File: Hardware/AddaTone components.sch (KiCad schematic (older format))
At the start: 82 parts, among them J1 SWD_Header, J2 Conn_01x20_Female, J3 Conn_01x20_Female, J8 Eurorack_16_pin_power, U1 STM32F446RETx, U2 ICE40UP5K-SG48ITR, U3 MCP6004, U4 PCM5100APW, U5 TL072, U6 LD1117S12TR_SOT223, U7 LM1117-3.3, Y1 ECS-12MHz

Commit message: Initial PCB Wiring Completed
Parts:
- C1, C15, C35, C4, C7, C9: footprint Capacitors_SMD:C_0805_HandSoldering -> Capacitors_SMD:C_0603_HandSoldering
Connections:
- net labels added: FPGA_SO
- wire segments 370 -> 367
- no-connect marks 54 -> 57

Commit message: Updated microcontroller code for correct ADC channels and implemented HSE oscillator output
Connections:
- net labels added: FREQ_SCALE_CV, HARM_COUNT_POT, PITCH_CV
- net labels removed: FREQ_SCALE, HARM_COUNT, V_OCT_CV
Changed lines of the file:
@@
 $EndComp
 Text GLabel 9750 2350 2    50   Input ~ 0
-V_OCT_CV
+PITCH_CV
 Wire Wire Line
 	9750 2350 9400 2350
@@
 	8350 3600 8400 3600
 Text GLabel 3400 2600 2    50   Input ~ 0
-V_OCT_CV
+PITCH_CV
 Text GLabel 1650 3900 0    50   Input ~ 0
 HARM1_CV
@@
 DAC2_OUT
 Text GLabel 3400 2200 2    50   Input ~ 0
-HARM_COUNT
+HARM_COUNT_POT
 $Comp
 L Amplifier_Operational:MCP6004 U3
@@
 $EndComp
 Text GLabel 9750 7950 2    50   Input ~ 0
-FREQ_SCALE
+FREQ_SCALE_CV
 Wire Wire Line
 	9750 6050 9400 6050
@@
 	15700 4600 15850 4600
 Text GLabel 3400 2700 2    50   Input ~ 0
-FREQ_SCALE
+FREQ_SCALE_CV
 Wire Wire Line
 	3250 2600 3400 2600
@@
 HARM2_POT
 Text GLabel 6250 1100 0    50   Input ~ 0
-HARM_COUNT
+HARM_COUNT_POT
 Text GLabel 6250 1300 0    50   Input ~ 0
 FTUNE

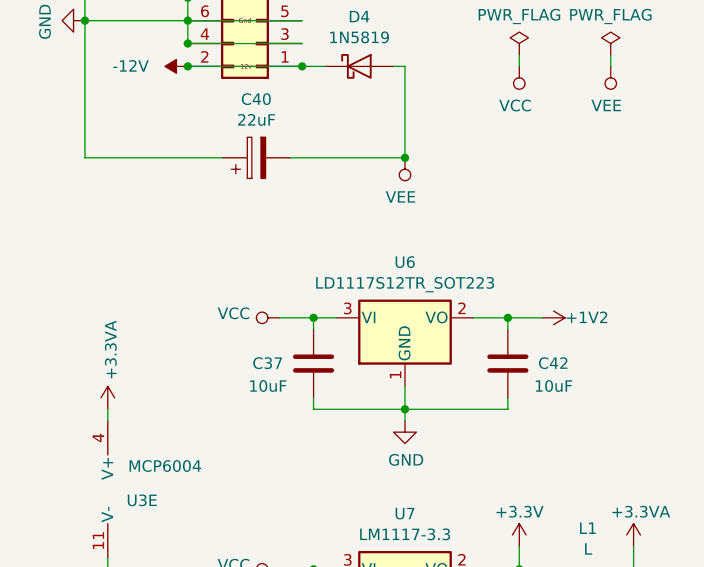
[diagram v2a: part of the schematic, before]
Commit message: Minor tweaks to PCB layout
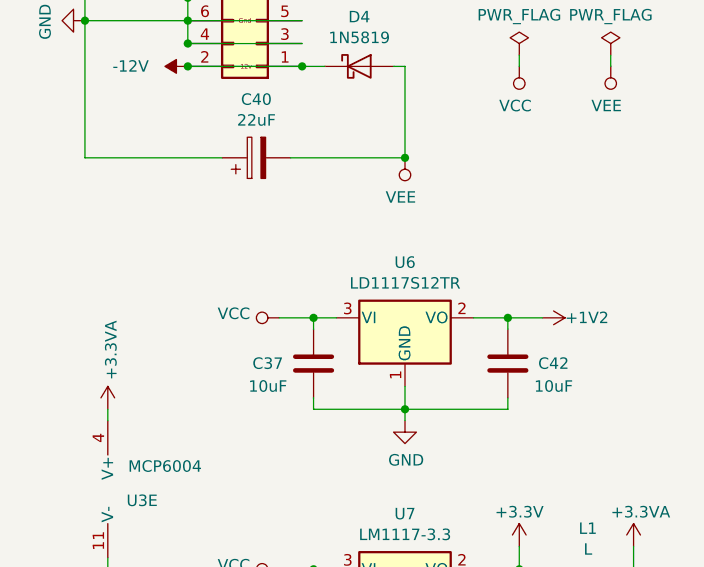
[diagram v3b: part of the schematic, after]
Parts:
- U6: value LD1117S12TR_SOT223 -> LD1117S12TR
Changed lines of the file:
@@
 P 15200 3500
 F 0 "U6" H 15200 3742 50  0000 C CNN
-F 1 "LD1117S12TR_SOT223" H 15200 3651 50  0000 C CNN
+F 1 "LD1117S12TR" H 15200 3651 50  0000 C CNN
 F 2 "TO_SOT_Packages_SMD:SOT-223" H 15200 3700 50  0001 C CNN
 F 3 "http://www.st.com/st-web-ui/static/active/en/resource/technical/document/datasheet/CD00000544.pdf" H 15300 3250 50  0001 C CNN

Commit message: Further refinements to PCB layout
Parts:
- removed J2, J3: Conn_01x20_Female, Socket_Strips:Socket_Strip_Straight_1x20_Pitch2.54mm, symbol Connector:Conn_01x20_Female
- added J2: Conn_01x10_Female, Socket_Strips:Socket_Strip_Straight_1x10_Pitch2.54mm, symbol Connector:Conn_01x10_Female
- added J3: Conn_01x12_Female, Socket_Strips:Socket_Strip_Straight_1x12_Pitch2.54mm, symbol Connector:Conn_01x12_Female
- added J4, J6: Conn_01x03_Male, Pin_Headers:Pin_Header_Straight_1x03_Pitch2.54mm, symbol Connector:Conn_01x03_Male
- added J5: Conn_01x06_Male, Pin_Headers:Pin_Header_Straight_2x03_Pitch2.54mm, symbol Connector:Conn_01x06_Male
- added TP1: TestPoint, Socket_Strips:Socket_Strip_Straight_1x01_Pitch2.54mm, symbol Connector:TestPoint
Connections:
- wire segments 367 -> 330

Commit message: Refinements to PCB
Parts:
- added J7: Conn_01x02_Male, Pin_Headers:Pin_Header_Straight_1x02_Pitch2.54mm, symbol Connector:Conn_01x02_Male
- added TP2, TP3, TP4, TP5, TP6: TestPoint, Pin_Headers:Pin_Header_Straight_1x01_Pitch2.54mm, symbol Connector:TestPoint
- added TP7: TestPoint, Measurement_Points:Test_Point_Keystone_5010-5014_Multipurpose, symbol Connector:TestPoint
- TP1: footprint Socket_Strips:Socket_Strip_Straight_1x01_Pitch2.54mm -> Pin_Headers:Pin_Header_Straight_1x01_Pitch2.54mm
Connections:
- net +1V2: now also TP3.1
- net +3.3VA: now also TP6.1
- net +3V3: now also TP2.1
- net GND: now also TP7.1
- net VCC: now also TP4.1
- net VEE: now also TP5.1
- net F_TEST1: now reaches U2.42 (IOT_51a)
- net F_TEST1: now also J7.1 (Pin_1)
- net F_TEST2: now reaches U2.45 (IOB_5b)
- net F_TEST2: now also J7.2 (Pin_2)
- no-connect marks 57 -> 55
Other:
- moved on the sheet: TP1
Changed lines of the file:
@@
 Text GLabel 1600 7300 0    50   Input ~ 0
 DAC_BCLK
-Text GLabel 2200 6300 1    50   Input ~ 0
+Text GLabel 2200 6350 1    50   Input ~ 0
 DAC_LRCLK
 Text GLabel 1600 7200 0    50   Input ~ 0
@@
 	1600 7300 1750 7300
 Wire Wire Line
-	2200 6300 2200 6450
+	2200 6350 2200 6450
 Text GLabel 3400 4800 2    50   Input ~ 0
 FPGA_SS
@@
 Text GLabel 2900 8750 3    50   Input ~ 0
 MCO2_CLOCK_OUT
-Text GLabel 3300 6300 1    50   Input ~ 0
+Text GLabel 3300 6350 1    50   Input ~ 0
 MIX_SWITCH
 Wire Wire Line
-	3300 6300 3300 6450
+	3300 6350 3300 6450
 Text GLabel 3900 8100 2    50   Input ~ 0
 RING_MOD
@@
 NoConn ~ 2600 6450
 NoConn ~ 2700 6450
-NoConn ~ 2800 6450
 NoConn ~ 2900 6450
 NoConn ~ 3000 6450
 NoConn ~ 3100 6450
 NoConn ~ 3200 6450
-NoConn ~ 2500 6450
 $Comp
 L Regulator_Linear:LM1117-3.3 U7
@@
 Text GLabel 6250 4050 0    50   Input ~ 0
 FPGA_SI
-Text GLabel 6250 5350 0    50   Input ~ 0
+Text GLabel 4900 5200 0    50   Input ~ 0
 MCO2_CLOCK_OUT
 Text GLabel 6150 3500 0    50   Input ~ 0
@@
 L Connector:TestPoint TP1
 U 1 1 5EE3114E
-P 6250 5350
-F 0 "TP1" V 6204 5538 50  0000 L CNN
-F 1 "TestPoint" V 6295 5538 50  0000 L CNN
-F 2 "Socket_Strips:Socket_Strip_Straight_1x01_Pitch2.54mm" H 6450 5350 50  0001 C CNN
-F 3 "~" H 6450 5350 50  0001 C CNN
-	1    6250 5350
+P 4900 5200
+F 0 "TP1" V 4854 5388 50  0000 L CNN
+F 1 "TestPoint" V 4945 5388 50  0000 L CNN
+F 2 "Pin_Headers:Pin_Header_Straight_1x01_Pitch2.54mm" H 5100 5200 50  0001 C CNN
+F 3 "~" H 5100 5200 50  0001 C CNN
+	1    4900 5200
 	0    1    1    0
 $EndComp
@@
 	1    0    0    -1
 $EndComp
+$Comp
+L Connector:TestPoint TP2
+U 1 1 5E9F4A5B
+P 4900 5400
+F 0 "TP2" V 4854 5588 50  0000 L CNN
+F 1 "TestPoint" V 4945 5588 50  0000 L CNN
+F 2 "Pin_Headers:Pin_Header_Straight_1x01_Pitch2.54mm" H 5100 5400 50  0001 C CNN
+F 3 "~" H 5100 5400 50  0001 C CNN
+	1    4900 5400
+	0    1    1    0
+$EndComp
+$Comp
+L power:+3.3V #PWR0106
+U 1 1 5E9F4C8E
+P 4900 5400
+F 0 "#PWR0106" H 4900 5250 50  0001 C CNN
+F 1 "+3.3V" V 4900 5650 50  0000 C CNN
+F 2 "" H 4900 5400 50  0001 C CNN
+F 3 "" H 4900 5400 50  0001 C CNN
+	1    4900 5400
+	0    -1   -1   0
+$EndComp
+$Comp
+L power:VEE #PWR0107
+U 1 1 5E9F8A32
+P 4900 6000
+F 0 "#PWR0107" H 4900 5850 50  0001 C CNN
+F 1 "VEE" V 4900 6200 50  0000 C CNN
+F 2 "" H 4900 6000 50  0001 C CNN
+F 3 "" H 4900 6000 50  0001 C CNN
+	1    4900 6000
+	0    -1   -1   0
+$EndComp
+$Comp
+L power:VCC #PWR0108
+U 1 1 5E9F8A38
+P 4900 5800
+F 0 "#PWR0108" H 4900 5650 50  0001 C CNN
+F 1 "VCC" V 4900 6000 50  0000 C CNN
+F 2 "" H 4900 5800 50  0001 C CNN
+F 3 "" H 4900 5800 50  0001 C CNN
+	1    4900 5800
+	0    -1   -1   0
+$EndComp
+$Comp
+L power:+3.3VA #PWR0109
+U 1 1 5EA18F72
+P 4900 6200
+F 0 "#PWR0109" H 4900 6050 50  0001 C CNN
+F 1 "+3.3VA" V 4900 6350 50  0000 L CNN
+F 2 "" H 4900 6200 50  0001 C CNN
+F 3 "" H 4900 6200 50  0001 C CNN
+	1    4900 6200
+	0    -1   -1   0
+$EndComp
+$Comp
+L power:+1V2 #PWR0110
+U 1 1 5EA1C9C4
+P 4900 5600
+F 0 "#PWR0110" H 4900 5450 50  0001 C CNN
+F 1 "+1V2" V 4900 5750 50  0000 L CNN
+F 2 "" H 4900 5600 50  0001 C CNN
+F 3 "" H 4900 5600 50  0001 C CNN
+	1    4900 5600
+	0    -1   -1   0
+$EndComp
+$Comp
+L Connector:TestPoint TP3
+U 1 1 5EAA1138
+P 4900 5600
+F 0 "TP3" V 4854 5788 50  0000 L CNN
+F 1 "TestPoint" V 4945 5788 50  0000 L CNN
+F 2 "Pin_Headers:Pin_Header_Straight_1x01_Pitch2.54mm" H 5100 5600 50  0001 C CNN
+F 3 "~" H 5100 5600 50  0001 C CNN
+	1    4900 5600
+	0    1    1    0
+$EndComp
+$Comp
+L Connector:TestPoint TP4
+U 1 1 5EAA13A1
+P 4900 5800
+F 0 "TP4" V 4854 5988 50  0000 L CNN
+F 1 "TestPoint" V 4945 5988 50  0000 L CNN
+F 2 "Pin_Headers:Pin_Header_Straight_1x01_Pitch2.54mm" H 5100 5800 50  0001 C CNN
+F 3 "~" H 5100 5800 50  0001 C CNN
+	1    4900 5800
+	0    1    1    0
+$EndComp
+$Comp
+L Connector:TestPoint TP5
+U 1 1 5EAA16DF
+P 4900 6000
+F 0 "TP5" V 4854 6188 50  0000 L CNN
+F 1 "TestPoint" V 4945 6188 50  0000 L CNN
+F 2 "Pin_Headers:Pin_Header_Straight_1x01_Pitch2.54mm" H 5100 6000 50  0001 C CNN
+F 3 "~" H 5100 6000 50  0001 C CNN
+	1    4900 6000
+	0    1    1    0
+$EndComp
+$Comp
+L Connector:TestPoint TP6
+U 1 1 5EAA1941
+P 4900 6200
+F 0 "TP6" V 4854 6388 50  0000 L CNN
+F 1 "TestPoint" V 4945 6388 50  0000 L CNN
+F 2 "Pin_Headers:Pin_Header_Straight_1x01_Pitch2.54mm" H 5100 6200 50  0001 C CNN
+F 3 "~" H 5100 6200 50  0001 C CNN
+	1    4900 6200
+	0    1    1    0
+$EndComp
+Text GLabel 2500 6350 1    50   Input ~ 0
+F_TEST2
+Text GLabel 2800 6350 1    50   Input ~ 0
+F_TEST1
+Wire Wire Line
+	2500 6350 2500 6450
+Wire Wire Line
+	2800 6350 2800 6450
+Text GLabel 6250 5050 0    50   Input ~ 0
+F_TEST2
+Text GLabel 6250 4950 0    50   Input ~ 0
+F_TEST1
+$Comp
+L Connector:Conn_01x02_Male J7
+U 1 1 5ED5DD59
+P 6450 4950
+F 0 "J7" H 6422 4924 50  0000 R CNN
+F 1 "Conn_01x02_Male" H 6422 4833 50  0000 R CNN
+F 2 "Pin_Headers:Pin_Header_Straight_1x02_Pitch2.54mm" H 6450 4950 50  0001 C CNN
+F 3 "~" H 6450 4950 50  0001 C CNN
+	1    6450 4950
+	-1   0    0    -1
+$EndComp
+$Comp
+L Connector:TestPoint TP7
+U 1 1 5EDAD09E
+P 4900 6400
+F 0 "TP7" V 4854 6588 50  0000 L CNN
+F 1 "TestPoint" V 4945 6588 50  0000 L CNN
+F 2 "Measurement_Points:Test_Point_Keystone_5010-5014_Multipurpose" H 5100 6400 50  0001 C CNN
+F 3 "~" H 5100 6400 50  0001 C CNN
+	1    4900 6400
+	0    1    1    0
+$EndComp
+$Comp
+L power:GND #PWR020
+U 1 1 5EDAD2B2
+P 4900 6400
+F 0 "#PWR020" H 4900 6150 50  0001 C CNN
+F 1 "GND" V 4900 6150 50  0000 C CNN
+F 2 "" H 4900 6400 50  0001 C CNN
+F 3 "" H 4900 6400 50  0001 C CNN
+	1    4900 6400
+	0    1    1    0
+$EndComp
 $EndSCHEMATC

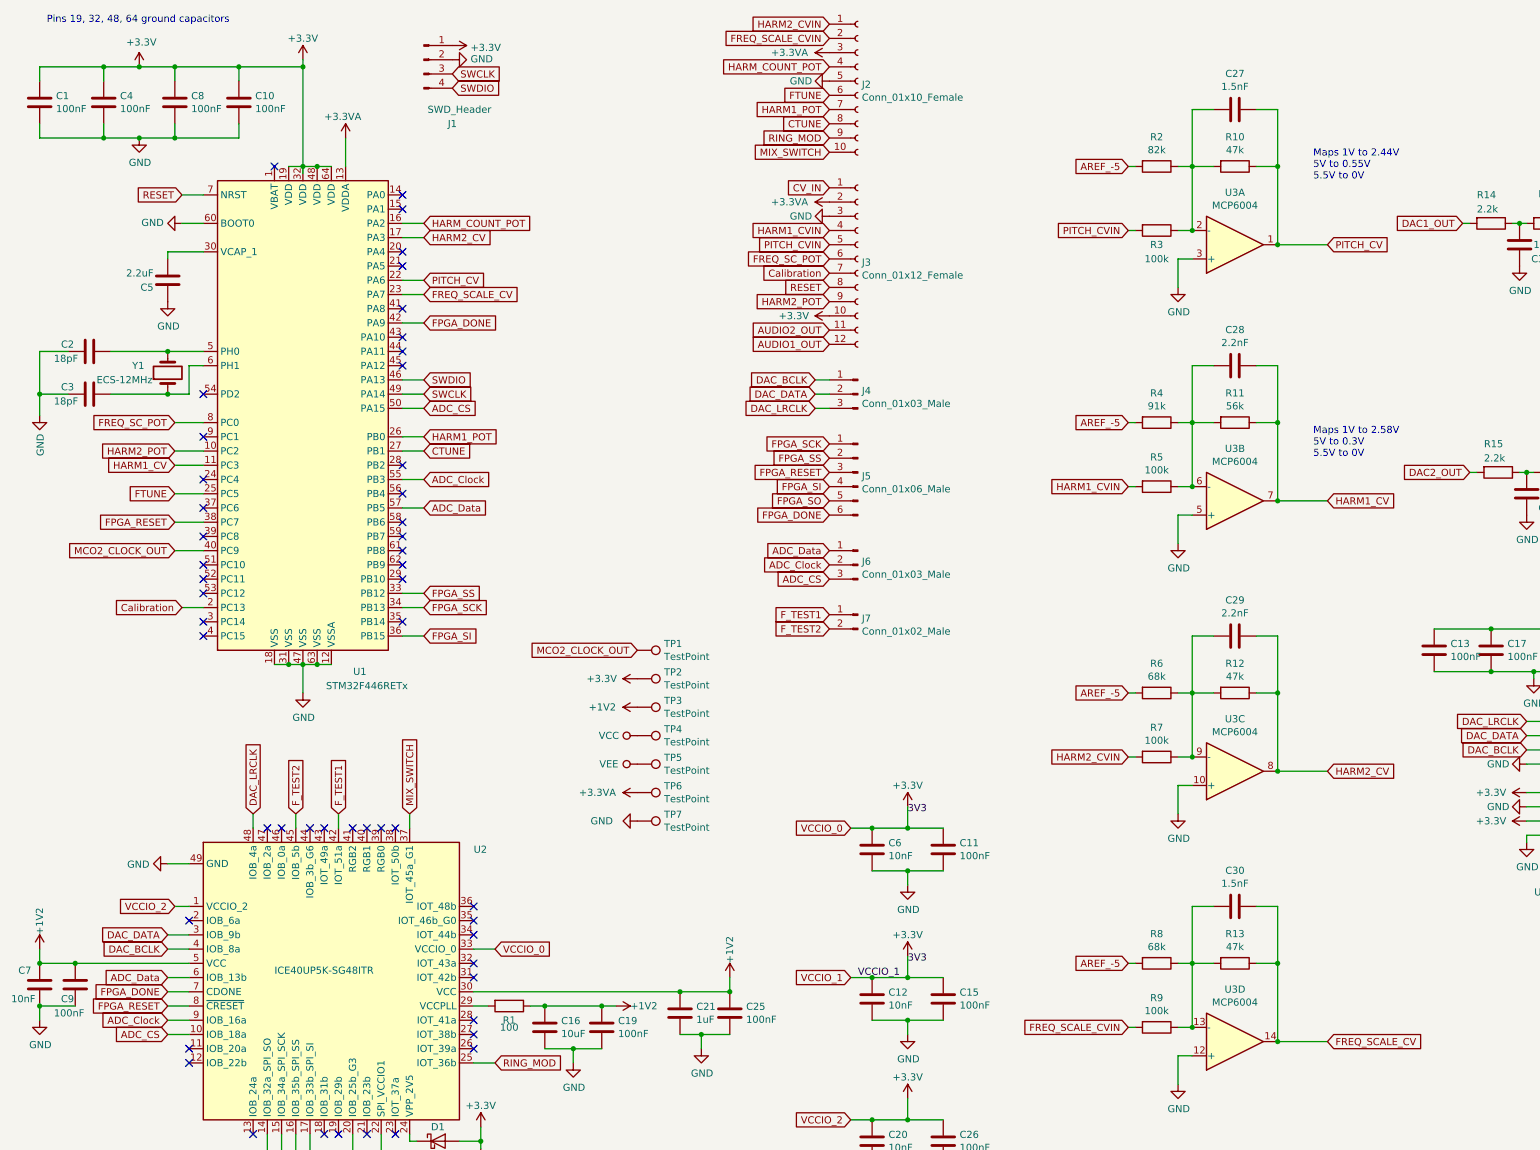
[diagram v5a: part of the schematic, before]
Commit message: Updated FPGA programming code to use correct pin for Reset; Minor PCB corrections
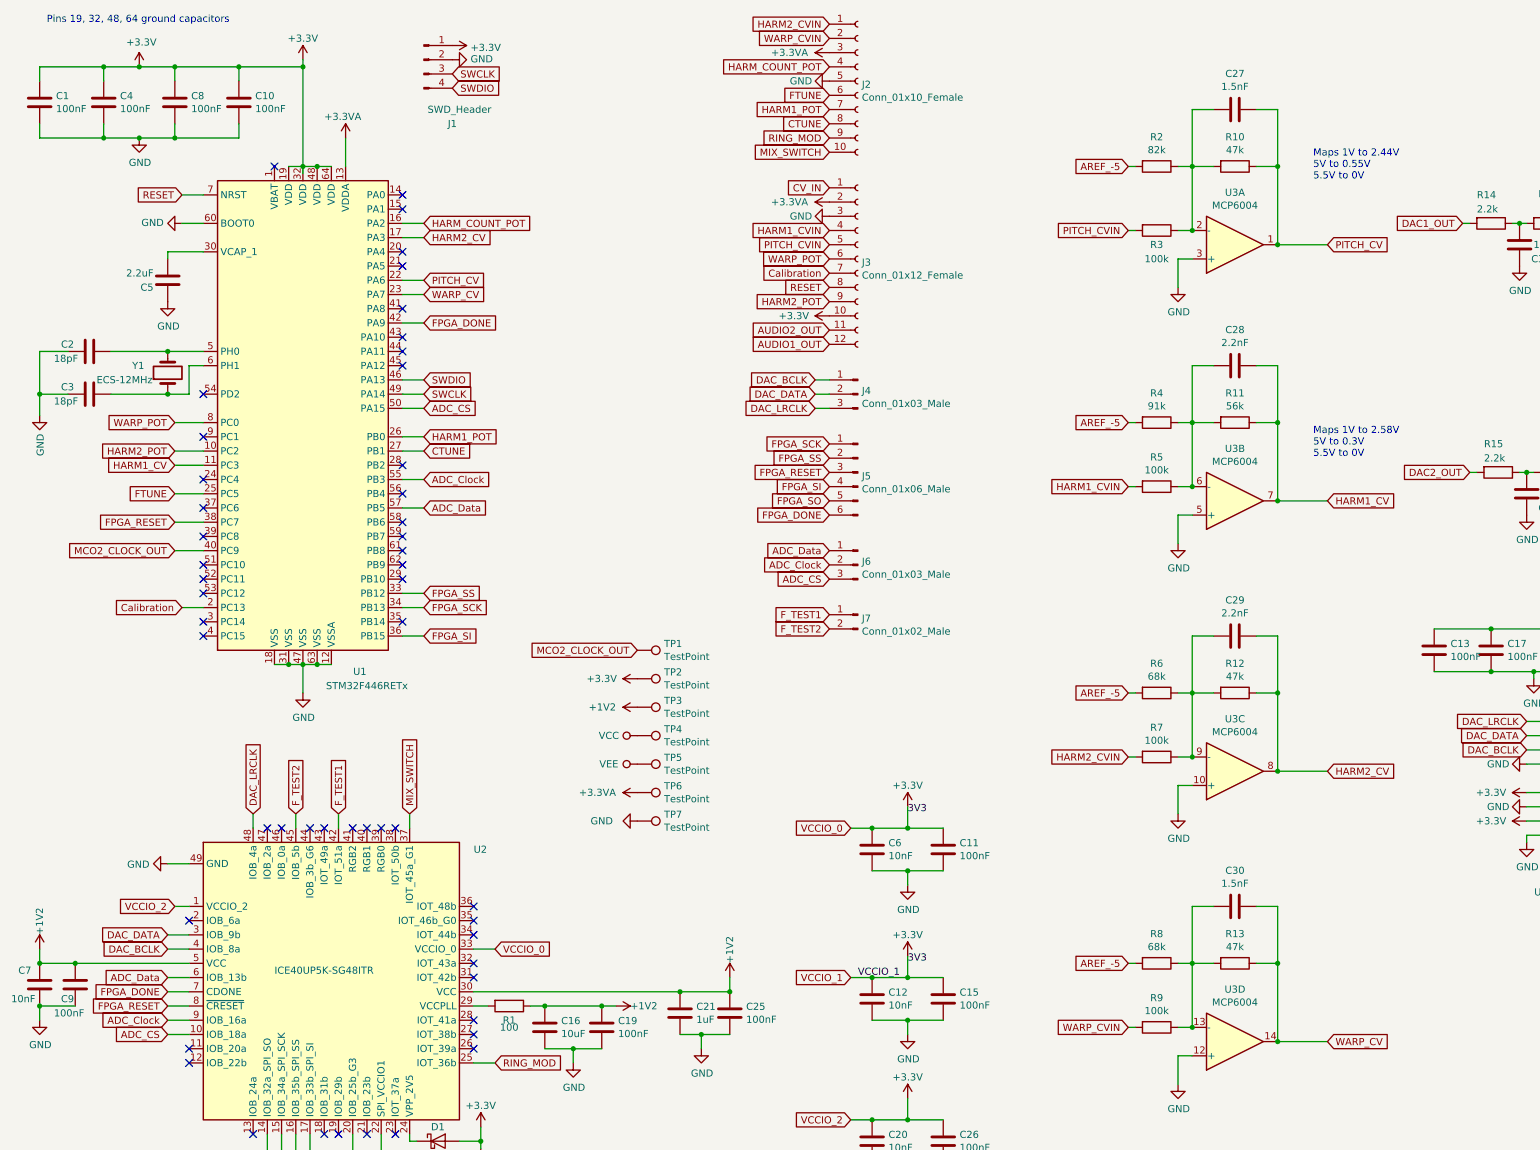
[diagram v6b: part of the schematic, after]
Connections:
- net FREQ_SCALE_CV renamed WARP_CV
- net FREQ_SCALE_CVIN renamed WARP_CVIN
- net FREQ_SC_POT renamed WARP_POT
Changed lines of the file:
@@
 $EndComp
 Text GLabel 9750 7950 2    50   Input ~ 0
-FREQ_SCALE_CV
+WARP_CV
 Wire Wire Line
 	9750 6050 9400 6050
@@
 	3250 3500 3400 3500
 Text GLabel 1650 3600 0    50   Input ~ 0
-FREQ_SC_POT
+WARP_POT
 Text GLabel 1650 4500 0    50   Input ~ 0
 MCO2_CLOCK_OUT
@@
 	15700 4600 15850 4600
 Text GLabel 3400 2700 2    50   Input ~ 0
-FREQ_SCALE_CV
+WARP_CV
 Wire Wire Line
 	3250 2600 3400 2600
@@
 CV_IN
 Text GLabel 6250 2450 0    50   Input ~ 0
-FREQ_SC_POT
+WARP_POT
 Text GLabel 6250 1500 0    50   Input ~ 0
 CTUNE
@@
 HARM2_CVIN
 Text GLabel 8350 7850 0    50   Input ~ 0
-FREQ_SCALE_CVIN
+WARP_CVIN
 Text GLabel 6250 2350 0    50   Input ~ 0
 PITCH_CVIN
@@
 	15200 5000 15700 5000
 Text GLabel 6250 900  0    50   Input ~ 0
-FREQ_SCALE_CVIN
+WARP_CVIN
 NoConn ~ 3250 2100
 NoConn ~ 3250 4500
